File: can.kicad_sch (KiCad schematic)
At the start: 15 parts, among them Q4 BSS84, U7 TCAN330, U8 MCP2515-xST, Y2 8MHz

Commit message: revised schematic after initial layout  - all connectors are vertical  - increased current handling of outputs  - replaced mechanical relay with ssr  - jumper to disable gps antenna power
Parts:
- C25: renamed from C24; footprint Capacitor_SMD:C_0603_1608Metric_Pad1.08x0.95mm_HandSolder -> Capacitor_SMD:C_0603_1608Metric
- C26: renamed from C25; footprint Capacitor_SMD:C_0603_1608Metric_Pad1.08x0.95mm_HandSolder -> Capacitor_SMD:C_0603_1608Metric
- C27: renamed from C26; footprint Capacitor_SMD:C_0603_1608Metric_Pad1.08x0.95mm_HandSolder -> Capacitor_SMD:C_0603_1608Metric
- C28: renamed from C27; footprint Capacitor_SMD:C_0603_1608Metric_Pad1.08x0.95mm_HandSolder -> Capacitor_SMD:C_0603_1608Metric
- D11: renamed from D12; footprint LED_SMD:LED_0603_1608Metric_Pad1.05x0.95mm_HandSolder -> LED_SMD:LED_0603_1608Metric
- R29: renamed from R28; footprint Resistor_SMD:R_0603_1608Metric_Pad0.98x0.95mm_HandSolder -> Resistor_SMD:R_0603_1608Metric
- R30: renamed from R29; footprint Resistor_SMD:R_0603_1608Metric_Pad0.98x0.95mm_HandSolder -> Resistor_SMD:R_0603_1608Metric
- R31: renamed from R30; footprint Resistor_SMD:R_0603_1608Metric_Pad0.98x0.95mm_HandSolder -> Resistor_SMD:R_0603_1608Metric
- renumbered D11 to D10, JP3 to JP4, JP4 to JP5
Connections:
- no-connect marks 6 -> 7
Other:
- moved on the sheet: C25, D11, JP4, Q4, R29, R31

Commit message: second pass at layout complete
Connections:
- net CANH: now also D10.2 (K2); no longer D10.1 (K1)
- net CANL: now also D10.1 (K1); no longer D10.2 (K2)
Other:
- moved on the sheet: D10
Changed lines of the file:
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@@
 	(symbol
 		(lib_id "Custom:PESD2CAN")
-		(at 231.14 74.93 0)
-		(mirror y)
+		(at 231.14 74.93 180)
 		(unit 1)
 		(exclude_from_sim no)
@@
 		(dnp no)
 		(property "Reference" "D10"
-			(at 231.0765 82.8845 0)
+			(at 231.0765 66.9755 0)
 			(effects
 				(font
@@
 		)
 		(property "Value" "PESD2CAN"
-			(at 231.0765 80.4602 0)
+			(at 231.0765 69.3998 0)
 			(effects
 				(font
@@
 		)
 		(property "Footprint" "Package_TO_SOT_SMD:SOT-23"
-			(at 231.14 82.55 0)
+			(at 231.14 67.31 0)
 			(effects
 				(font
@@
 		)
 		(property "Datasheet" ""
-			(at 229.87 72.39 0)
+			(at 229.87 77.47 0)
 			(effects
 				(font

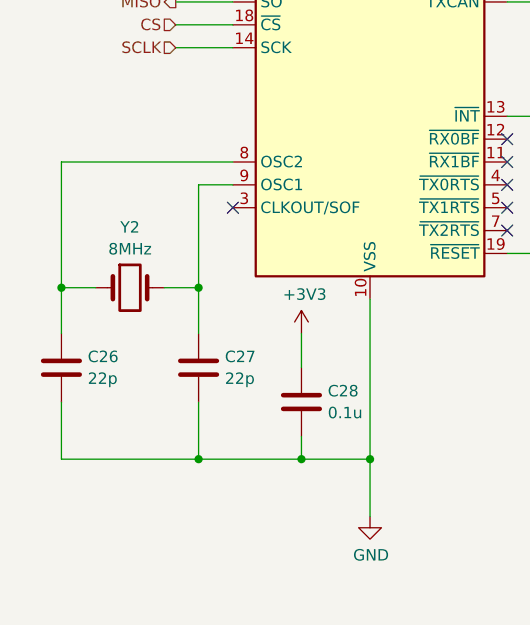
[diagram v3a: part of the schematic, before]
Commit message: add a version, add uart test pads to gps, sent for manufacturing
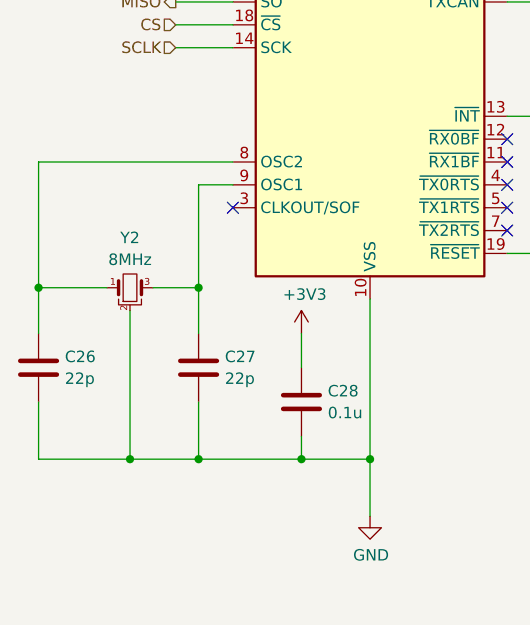
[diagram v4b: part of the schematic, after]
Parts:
- Q4: Mfg Part Number BSS84 -> 2N7002
- Y2: symbol Device:Crystal -> Device:Crystal_GND2_Small
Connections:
- net GND: now also Y2.2
- net at C27.1, U8.9 (OSC1): now also Y2.3; no longer Y2.2
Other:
- moved on the sheet: C26
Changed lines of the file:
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@@
 	)
 	(junction
-		(at 72.39 101.6)
+		(at 69.85 101.6)
 		(diameter 0)
 		(color 0 0 0 0)
@@
 	)
 	(junction
+		(at 80.01 120.65)
+		(diameter 0)
+		(color 0 0 0 0)
+	)
+	(junction
 		(at 87.63 101.6)
 		(diameter 0)
@@
 	(wire
 		(pts
-			(xy 83.82 101.6) (xy 87.63 101.6)
-		)
-		(stroke
-			(width 0)
-			(type default)
-		)
-	)
-	(wire
-		(pts
 			(xy 121.92 67.31) (xy 144.78 67.31)
 		)
@@
 	(wire
 		(pts
+			(xy 80.01 120.65) (xy 87.63 120.65)
+		)
+		(stroke
+			(width 0)
+			(type default)
+		)
+	)
+	(wire
+		(pts
 			(xy 87.63 120.65) (xy 87.63 114.3)
 		)
@@
 	(wire
 		(pts
-			(xy 72.39 101.6) (xy 76.2 101.6)
+			(xy 69.85 101.6) (xy 77.47 101.6)
 		)
 		(stroke
@@
 	(wire
 		(pts
-			(xy 72.39 87.63) (xy 91.44 87.63)
+			(xy 69.85 87.63) (xy 91.44 87.63)
 		)
 		(stroke
@@
 	(wire
 		(pts
+			(xy 80.01 104.14) (xy 80.01 120.65)
+		)
+		(stroke
+			(width 0)
+			(type default)
+		)
+	)
+	(wire
+		(pts
 			(xy 219.71 87.63) (xy 248.92 87.63)
 		)
@@
 	(wire
 		(pts
+			(xy 82.55 101.6) (xy 87.63 101.6)
+		)
+		(stroke
+			(width 0)
+			(type default)
+		)
+	)
+	(wire
+		(pts
 			(xy 144.78 113.03) (xy 144.78 72.39)
 		)
@@
 	(wire
 		(pts
-			(xy 72.39 114.3) (xy 72.39 120.65)
+			(xy 69.85 114.3) (xy 69.85 120.65)
 		)
 		(stroke
@@
 	(wire
 		(pts
-			(xy 72.39 106.68) (xy 72.39 101.6)
+			(xy 69.85 106.68) (xy 69.85 101.6)
 		)
 		(stroke
@@
 	(wire
 		(pts
-			(xy 72.39 120.65) (xy 87.63 120.65)
-		)
-		(stroke
-			(width 0)
-			(type default)
-		)
-	)
-	(wire
-		(pts
-			(xy 72.39 101.6) (xy 72.39 87.63)
+			(xy 69.85 120.65) (xy 80.01 120.65)
+		)
+		(stroke
+			(width 0)
+			(type default)
+		)
+	)
+	(wire
+		(pts
+			(xy 69.85 101.6) (xy 69.85 87.63)
 		)
 		(stroke
@@
 	)
 	(symbol
-		(lib_id "Device:Crystal")
+		(lib_id "Device:Crystal_GND2_Small")
 		(at 80.01 101.6 0)
 		(unit 1)
@@
 		(fields_autoplaced yes)
 		(property "Reference" "Y2"
-			(at 80.01 94.8901 0)
+			(at 80.01 96.0585 0)
 			(effects
 				(font
@@
 		)
 		(property "Value" "8MHz"
-			(at 80.01 97.3144 0)
+			(at 80.01 98.4828 0)
 			(effects
 				(font
@@
 			)
 		)
-		(property "Description" "Two pin crystal"
+		(property "Description" "Three pin crystal, GND on pin 2, small symbol"
 			(at 80.01 101.6 0)
 			(effects
@@
 		)
 		(pin "2"
+		)
+		(pin "3"
 		)
 		(instances
@@
 	(symbol
 		(lib_id "Device:C")
-		(at 72.39 110.49 0)
+		(at 69.85 110.49 0)
 		(unit 1)
 		(exclude_from_sim no)
@@
 		(fields_autoplaced yes)
 		(property "Reference" "C26"
-			(at 75.311 109.2778 0)
+			(at 72.771 109.2778 0)
 			(effects
 				(font
@@
 		)
 		(property "Value" "22p"
-			(at 75.311 111.7021 0)
+			(at 72.771 111.7021 0)
 			(effects
 				(font
@@
 		)
 		(property "Footprint" "Capacitor_SMD:C_0603_1608Metric"
-			(at 73.3552 114.3 0)
+			(at 70.8152 114.3 0)
 			(effects
 				(font
@@
 		)
 		(property "Datasheet" "~"
-			(at 72.39 110.49 0)
+			(at 69.85 110.49 0)
 			(effects
 				(font
@@
 		)
 		(property "Description" "Unpolarized capacitor"
-			(at 72.39 110.49 0)
+			(at 69.85 110.49 0)
 			(effects
 				(font
@@
 		)
 		(property "Mfg Part Number" "VJ0603A220KXAAC"
-			(at 72.39 110.49 0)
+			(at 69.85 110.49 0)
 			(effects
 				(font
@@
 			)
 		)
-		(property "Mfg Part Number" "BSS84"
+		(property "Mfg Part Number" "2N7002"
 			(at 160.02 113.03 0)
 			(effects

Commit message: bug fixes from testing
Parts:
- Q4: Mfg Part Number 2N7002 -> BSS84
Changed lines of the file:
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@@
 			)
 		)
-		(property "Mfg Part Number" "2N7002"
+		(property "Mfg Part Number" "BSS84"
 			(at 160.02 113.03 0)
 			(effects

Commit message: fixes from testing, updated for pi5
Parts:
- U8: symbol Interface_CAN_LIN:MCP2515-xST -> Custom:MCP2515-xML
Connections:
- net +3V3: now also U8.18 (VDD); no longer U8.20 (VDD)
- net CS: now also U8.16 (~{CS}); no longer U8.18 (~{CS})
- net INT: now also U8.11 (~{INT}); no longer U8.13 (~{INT})
- net MISO: now also U8.15 (SO); no longer U8.17 (SO)
- net MOSI: now also U8.14 (SI); no longer U8.16 (SI)
- net SCLK: now also U8.12 (SCK); no longer U8.14 (SCK)
- net at U8.1 (CLKOUT/SOF): no longer U7.1 (TXD)
- net at R30.1: now also U8.17 (~{RESET}); no longer U8.19 (~{RESET})
- net at Q4.1 (G), U7.4 (RXD): now also U8.20 (RXCAN); no longer U8.2 (RXCAN)
- net at U8.6 (OSC2): now also C26.1, Y2.1
- net at U8.7 (OSC1): now also C27.1, Y2.3
- net GND renamed EP
- net EP: now also U8.21 (EP), U8.8 (VSS); no longer U8.10 (VSS)
- new net: U7.1 (TXD), U8.19 (TXCAN)
- now unconnected: U8.9 (OSC1)
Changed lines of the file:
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@@
 	)
 	(symbol
-		(lib_id "Interface_CAN_LIN:MCP2515-xST")
+		(lib_id "Custom:MCP2515-xML")
 		(at 106.68 82.55 0)
 		(unit 1)
@@
 			)
 		)
-		(property "Datasheet" "http://ww1.microchip.com/downloads/en/DeviceDoc/21801e.pdf"
+		(property "Datasheet" "https://ww1.microchip.com/downloads/aemDocuments/documents/APID/ProductDocuments/DataSheets/MCP2515-Family-Data-Sheet-DS20001801K.pdf"
 			(at 109.22 102.87 0)
 			(effects
@@
 			)
 		)
-		(property "Description" "Stand-Alone CAN Controller with SPI Interface, TSSOP-20"
+		(property "Description" "Stand-Alone CAN Controller with SPI Interface, QFN-20"
 			(at 106.68 82.55 0)
 			(effects
@@
 		(pin "17"
 		)
+		(pin "21"
+		)
 		(instances

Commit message: switch can crystal to 12MHz
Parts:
- Y2: value 8MHz -> 12MHz; Mfg Part Number FL0800008Q -> FL1200112
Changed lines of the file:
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@@
 			)
 		)
-		(property "Value" "8MHz"
+		(property "Value" "12MHz"
 			(at 80.01 98.4828 0)
 			(effects
@@
 			)
 		)
-		(property "Mfg Part Number" "FL0800008Q"
+		(property "Mfg Part Number" "FL1200112"
 			(at 80.01 101.6 0)
 			(effects

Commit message: update resistors to more commmon values
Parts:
- R31: value 220 -> 270
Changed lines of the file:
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@@
 			)
 		)
-		(property "Value" "220"
+		(property "Value" "270"
 			(at 164.338 128.2121 0)
 			(effects
